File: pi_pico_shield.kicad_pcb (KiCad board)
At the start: 2 copper layers, 55 x 80 mm, 17 parts, among them U1 Pico

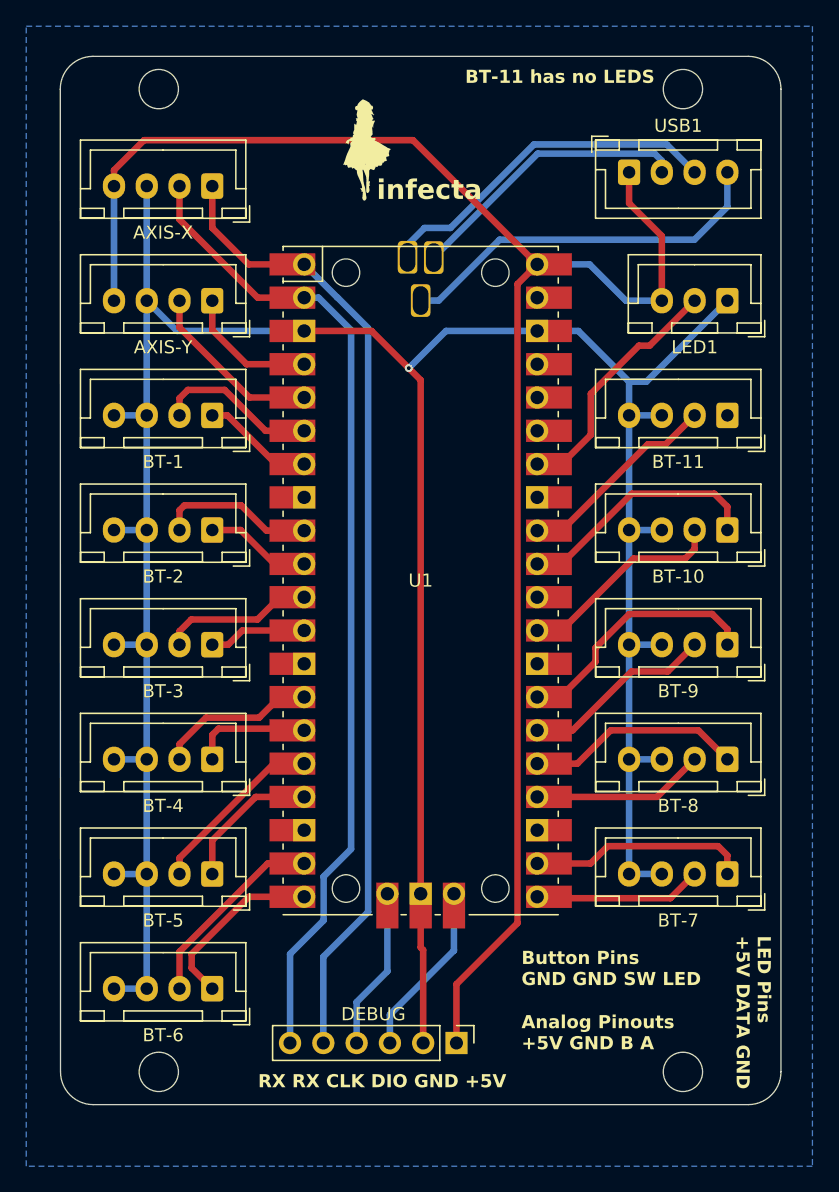
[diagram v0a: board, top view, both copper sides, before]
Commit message: Fix duplicate RX silkscreens. Clean up traces. Update Gerbers
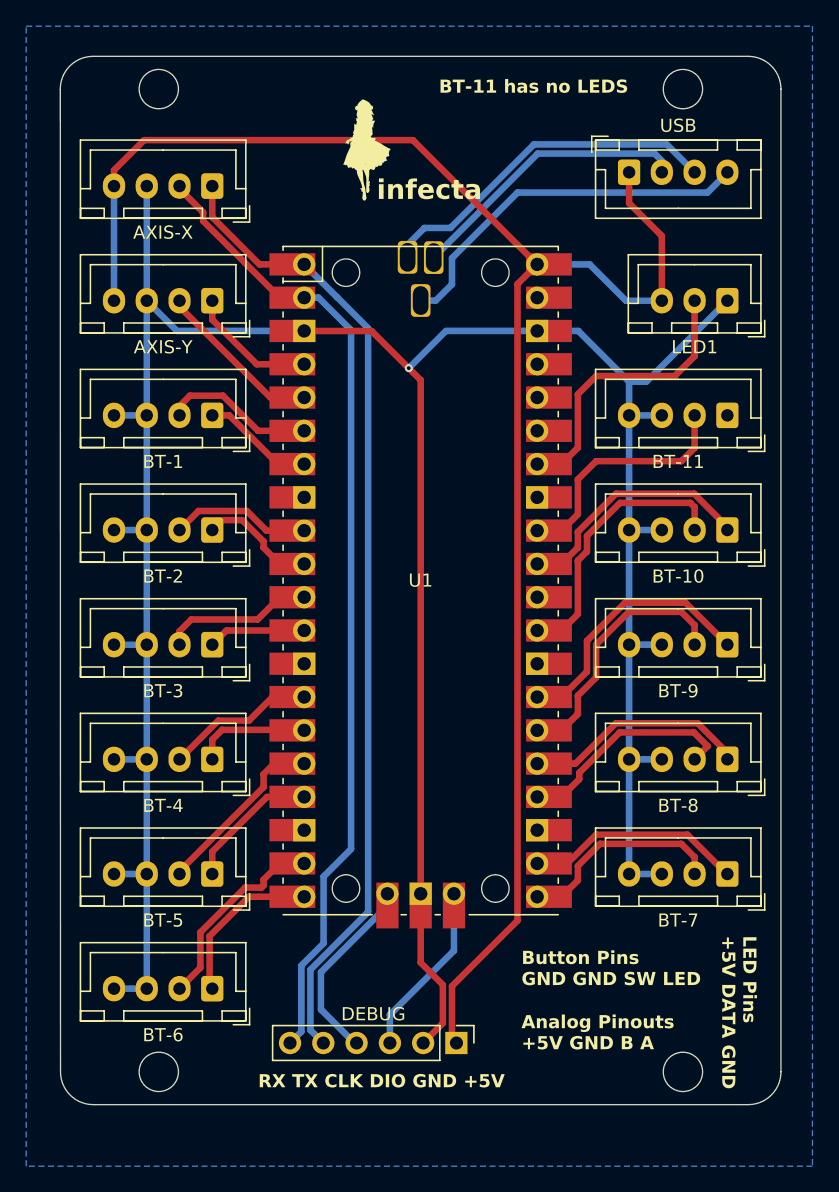
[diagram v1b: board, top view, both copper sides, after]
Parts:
- renumbered USB1 to USB
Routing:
- net BT-9_SW: track 14.7 -> 20.0 mm
- net BT-10_SW: track 16.0 -> 21.0 mm
- net BT-8_SW: track 13.2 -> 17.2 mm
- net BT-7_SW: track 12.8 -> 16.2 mm
- net LED-WS2812B: track 19.0 -> 22.0 mm
- net BT-11_SW: track 15.7 -> 18.7 mm
- net SWCLK: track 12.4 -> 14.7 mm
- net GND: track 230.3 -> 231.5 mm
- net BT-2_SW: track 12.0 -> 10.8 mm
- net BT-6_LED: track 13.7 -> 12.6 mm
- net AXIS-X_B: track 75.5 -> 74.5 mm
- net AXIS-Y_B: track 13.8 -> 12.8 mm
- net BT-2_LED: track 8.09 -> 8.99 mm
- net BT-9_LED: track 19.4 -> 20.2 mm
- net BT-8_LED: track 16.5 -> 17.2 mm
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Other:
- board text added: "RX TX CLK DIO GND +5V"
- board text removed: "RX RX CLK DIO GND +5V"
